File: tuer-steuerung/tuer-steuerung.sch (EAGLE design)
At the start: 47 parts, among them IC1 L6203, IC2 MEGA8-P, Q1 16Mhz, T1 BC337, T2 BC337

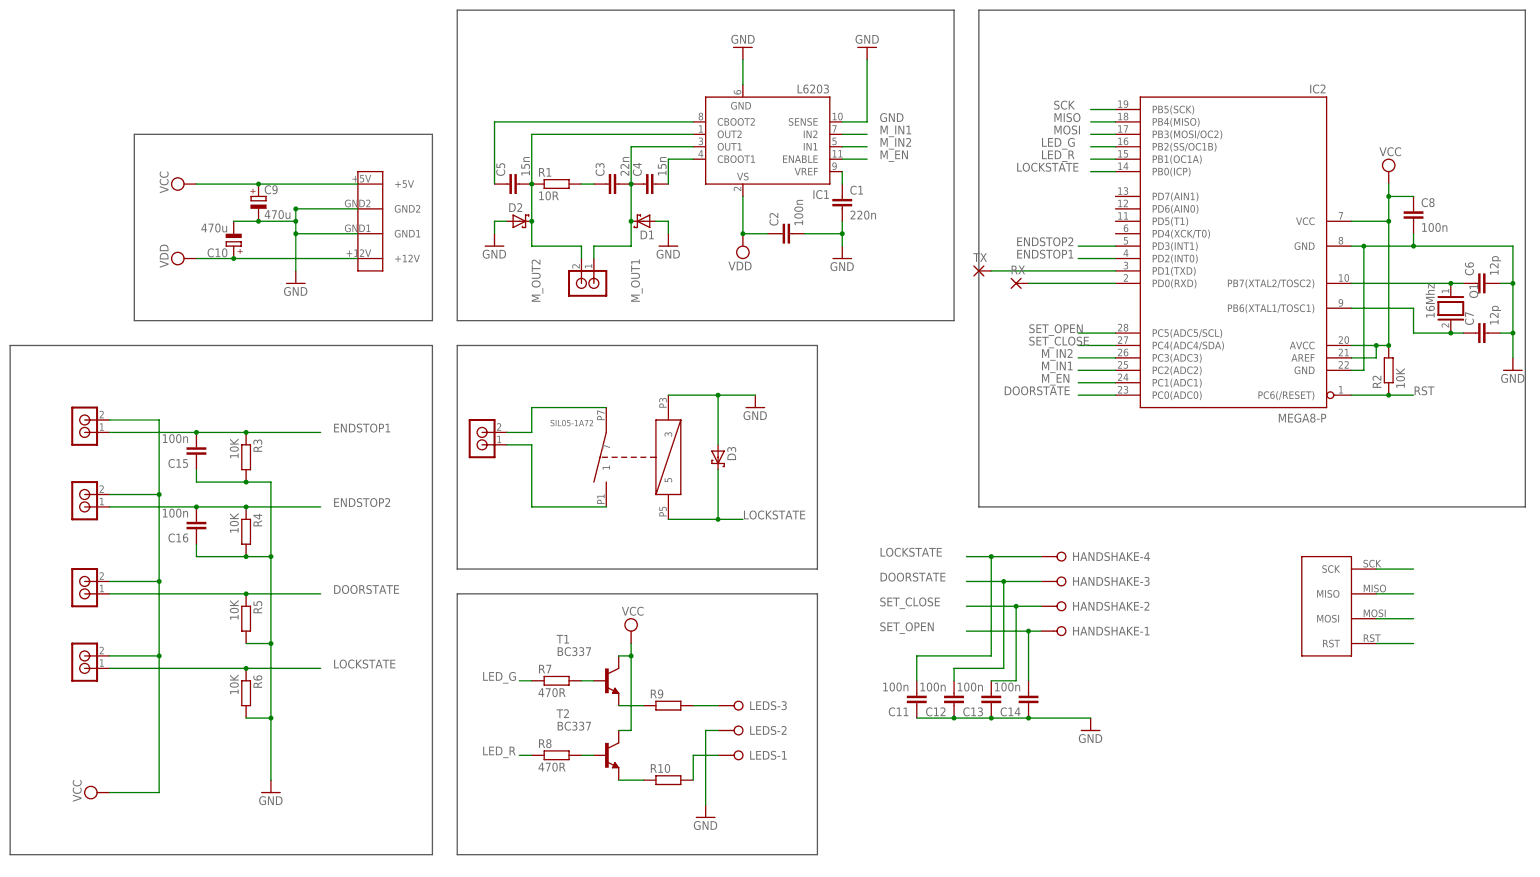
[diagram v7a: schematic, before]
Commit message: Anschlussklemmen durch die richtigen Typen ersetzt und Mini-Tweaks
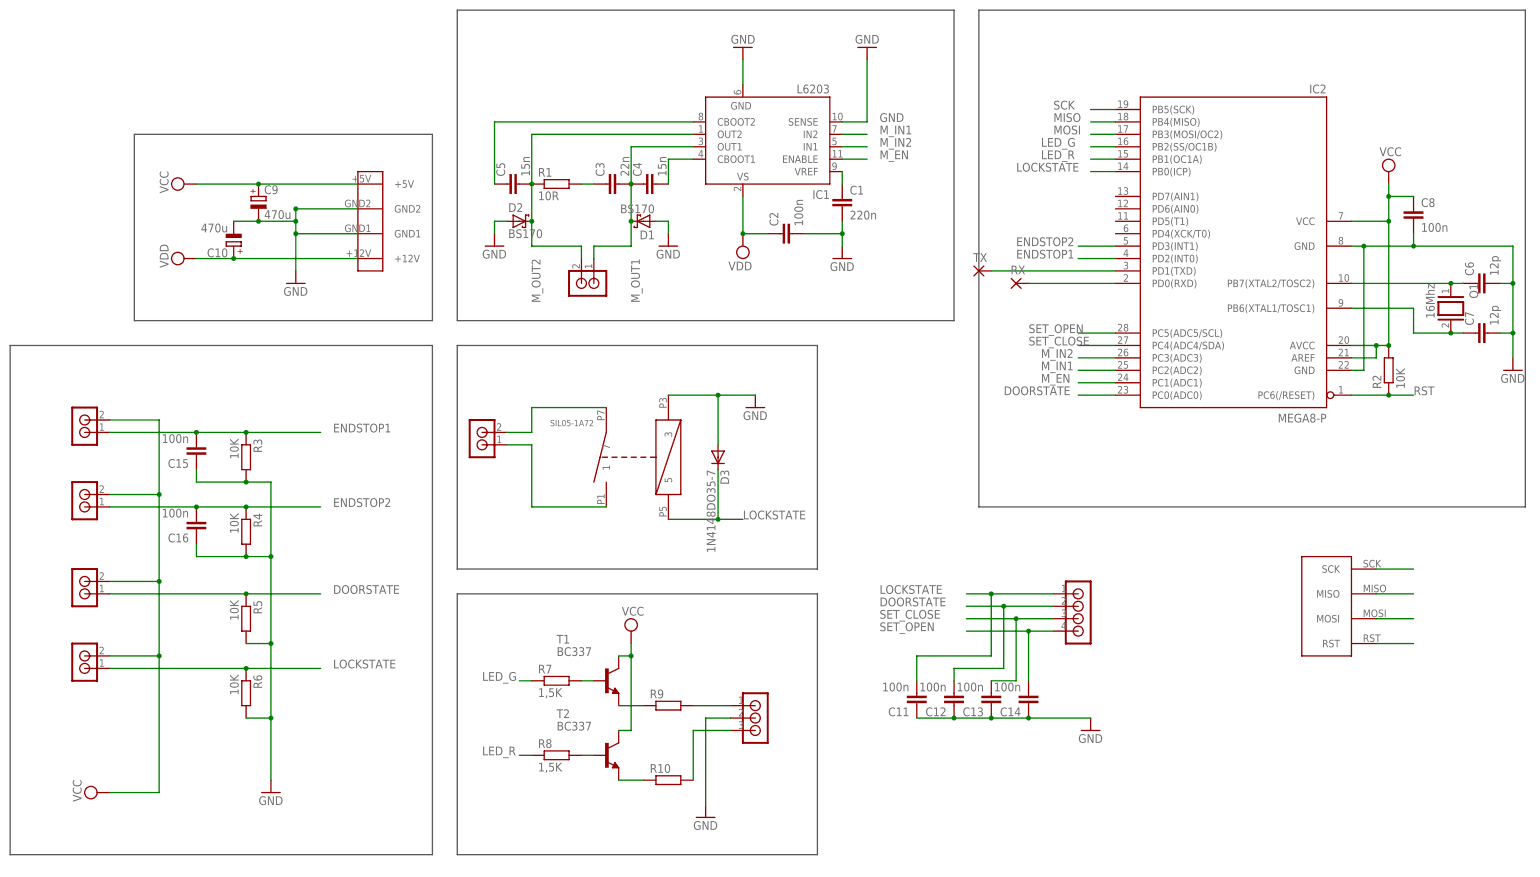
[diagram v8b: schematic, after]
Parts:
- removed HANDSHAKE: (no value), con-wago-508:W237-04P
- removed LEDS: (no value), con-wago-508:W237-03P
- added U$4: RIACON_101_3, n39:RIACON_101_3
- added U$5: RIACON_101_4, n39:RIACON_101_4
- D1, D2: value (none) -> BS170
- D3: value (none) -> 1N4148DO35-7; device diode:SCHOTTKY-DIODEDO35-7 -> diode:1N4148DO35-7
- R7, R8: value 470R -> 1,5K
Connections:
- net DOORSTATE: now also U$5.2; no longer HANDSHAKE-3.KL
- net GND: now also U$4.2; no longer LEDS-2.KL
- net LOCKSTATE: now also U$5.1; no longer HANDSHAKE-4.KL
- net N$12: now also U$4.1; no longer LEDS-3.KL
- net N$14: now also U$4.3; no longer LEDS-1.KL
- net SET_CLOSE: now also U$5.3; no longer HANDSHAKE-2.KL
- net SET_OPEN: now also U$5.4; no longer HANDSHAKE-1.KL
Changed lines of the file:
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@@
 <part name="IC2" library="atmel" deviceset="MEGA8-P" device=""/>
 <part name="Q1" library="special" deviceset="XTAL/S" device="" value="16Mhz"/>
-<part name="D1" library="diode" deviceset="SCHOTTKY-DIODE" device="DO35-7"/>
-<part name="D2" library="diode" deviceset="SCHOTTKY-DIODE" device="DO35-7"/>
+<part name="D1" library="diode" deviceset="SCHOTTKY-DIODE" device="DO35-7" value="BS170"/>
+<part name="D2" library="diode" deviceset="SCHOTTKY-DIODE" device="DO35-7" value="BS170"/>
 <part name="GND1" library="supply1" deviceset="GND" device=""/>
 <part name="SUPPLY1" library="supply2" deviceset="VDD" device=""/>
@@
 <part name="R6" library="resistor" deviceset="R-EU_" device="0204/5" value="10K"/>
 <part name="U$2" library="n39" deviceset="SIL05-1A72" device=""/>
-<part name="D3" library="diode" deviceset="SCHOTTKY-DIODE" device="DO35-7"/>
+<part name="D3" library="diode" deviceset="1N4148" device="DO35-7"/>
 <part name="GND9" library="supply1" deviceset="GND" device=""/>
 <part name="T1" library="transistor" deviceset="BC337" device=""/>
 <part name="T2" library="transistor" deviceset="BC337" device=""/>
-<part name="R7" library="resistor" deviceset="R-EU_" device="0204/5" value="470R"/>
-<part name="R8" library="resistor" deviceset="R-EU_" device="0204/5" value="470R"/>
-<part name="LEDS" library="con-wago-508" deviceset="W237-03P" device=""/>
+<part name="R7" library="resistor" deviceset="R-EU_" device="0204/5" value="1,5K"/>
+<part name="R8" library="resistor" deviceset="R-EU_" device="0204/5" value="1,5K"/>
 <part name="GND10" library="supply1" deviceset="GND" device=""/>
-<part name="HANDSHAKE" library="con-wago-508" deviceset="W237-04P" device=""/>
 <part name="R9" library="resistor" deviceset="R-EU_" device="0207/2V"/>
 <part name="R10" library="resistor" deviceset="R-EU_" device="0207/2V"/>
@@
 <part name="NERDSTERN" library="n39" deviceset="RIACON_101_2" device=""/>
 <part name="GND8" library="supply1" deviceset="GND" device=""/>
+<part name="U$4" library="n39" deviceset="RIACON_101_3" device=""/>
+<part name="U$5" library="n39" deviceset="RIACON_101_4" device=""/>
 </parts>
 <sheets>
@@
 <instance part="R7" gate="G$1" x="7.62" y="-66.04"/>
 <instance part="R8" gate="G$1" x="7.62" y="-81.28"/>
-<instance part="LEDS" gate="-1" x="45.72" y="-81.28" rot="R180"/>
-<instance part="LEDS" gate="-2" x="45.72" y="-76.2" rot="R180"/>
-<instance part="LEDS" gate="-3" x="45.72" y="-71.12" rot="R180"/>
 <instance part="GND10" gate="1" x="38.1" y="-93.98"/>
-<instance part="HANDSHAKE" gate="-1" x="111.76" y="-55.88" rot="R180"/>
-<instance part="HANDSHAKE" gate="-2" x="111.76" y="-50.8" rot="R180"/>
-<instance part="HANDSHAKE" gate="-3" x="111.76" y="-45.72" rot="R180"/>
-<instance part="HANDSHAKE" gate="-4" x="111.76" y="-40.64" rot="R180"/>
 <instance part="R9" gate="G$1" x="30.48" y="-71.12"/>
 <instance part="R10" gate="G$1" x="30.48" y="-86.36"/>
@@
 <instance part="NERDSTERN" gate="G$1" x="-7.62" y="-17.78" rot="R180"/>
 <instance part="GND8" gate="1" x="71.12" y="63.5" rot="R180"/>
+<instance part="U$4" gate="G$1" x="48.26" y="-73.66"/>
+<instance part="U$5" gate="G$1" x="114.3" y="-53.34"/>
 </instances>
 <busses>
@@
 <segment>
 <pinref part="GND10" gate="1" pin="GND"/>
-<wire x1="38.1" y1="-91.44" x2="38.1" y2="-76.2" width="0.1524" layer="91"/>
-<pinref part="LEDS" gate="-2" pin="KL"/>
-<wire x1="38.1" y1="-76.2" x2="40.64" y2="-76.2" width="0.1524" layer="91"/>
+<wire x1="38.1" y1="-91.44" x2="38.1" y2="-73.66" width="0.1524" layer="91"/>
+<pinref part="U$4" gate="G$1" pin="2"/>
+<wire x1="38.1" y1="-73.66" x2="43.18" y2="-73.66" width="0.1524" layer="91"/>
 </segment>
 <segment>
@@
 </segment>
 <segment>
-<pinref part="HANDSHAKE" gate="-3" pin="KL"/>
-<wire x1="106.68" y1="-45.72" x2="99.06" y2="-45.72" width="0.1524" layer="91"/>
-<label x="73.66" y="-45.72" size="1.778" layer="95"/>
+<wire x1="109.22" y1="-50.8" x2="99.06" y2="-50.8" width="0.1524" layer="91"/>
+<label x="73.66" y="-50.8" size="1.778" layer="95"/>
 <pinref part="C12" gate="G$1" pin="2"/>
-<wire x1="99.06" y1="-45.72" x2="91.44" y2="-45.72" width="0.1524" layer="91"/>
+<wire x1="99.06" y1="-50.8" x2="91.44" y2="-50.8" width="0.1524" layer="91"/>
 <wire x1="88.9" y1="-66.04" x2="88.9" y2="-63.5" width="0.1524" layer="91"/>
 <wire x1="88.9" y1="-63.5" x2="99.06" y2="-63.5" width="0.1524" layer="91"/>
-<wire x1="99.06" y1="-63.5" x2="99.06" y2="-45.72" width="0.1524" layer="91"/>
-<junction x="99.06" y="-45.72"/>
+<wire x1="99.06" y1="-63.5" x2="99.06" y2="-50.8" width="0.1524" layer="91"/>
+<junction x="99.06" y="-50.8"/>
+<pinref part="U$5" gate="G$1" pin="2"/>
 </segment>
 </net>
@@
 </segment>
 <segment>
-<pinref part="HANDSHAKE" gate="-4" pin="KL"/>
-<wire x1="106.68" y1="-40.64" x2="96.52" y2="-40.64" width="0.1524" layer="91"/>
-<label x="73.66" y="-40.64" size="1.778" layer="95"/>
+<wire x1="109.22" y1="-48.26" x2="96.52" y2="-48.26" width="0.1524" layer="91"/>
+<label x="73.66" y="-48.26" size="1.778" layer="95"/>
 <pinref part="C11" gate="G$1" pin="2"/>
-<wire x1="96.52" y1="-40.64" x2="91.44" y2="-40.64" width="0.1524" layer="91"/>
+<wire x1="96.52" y1="-48.26" x2="91.44" y2="-48.26" width="0.1524" layer="91"/>
 <wire x1="81.28" y1="-66.04" x2="81.28" y2="-60.96" width="0.1524" layer="91"/>
 <wire x1="81.28" y1="-60.96" x2="96.52" y2="-60.96" width="0.1524" layer="91"/>
-<wire x1="96.52" y1="-60.96" x2="96.52" y2="-40.64" width="0.1524" layer="91"/>
-<junction x="96.52" y="-40.64"/>
+<wire x1="96.52" y1="-60.96" x2="96.52" y2="-48.26" width="0.1524" layer="91"/>
+<junction x="96.52" y="-48.26"/>
+<pinref part="U$5" gate="G$1" pin="1"/>
 </segment>
 <segment>
@@
 <net name="SET_OPEN" class="0">
 <segment>
-<pinref part="HANDSHAKE" gate="-1" pin="KL"/>
-<wire x1="106.68" y1="-55.88" x2="104.14" y2="-55.88" width="0.1524" layer="91"/>
 <label x="73.66" y="-55.88" size="1.778" layer="95"/>
 <pinref part="C14" gate="G$1" pin="2"/>
@@
 <wire x1="104.14" y1="-66.04" x2="104.14" y2="-55.88" width="0.1524" layer="91"/>
 <junction x="104.14" y="-55.88"/>
+<pinref part="U$5" gate="G$1" pin="4"/>
+<wire x1="104.14" y1="-55.88" x2="109.22" y2="-55.88" width="0.1524" layer="91"/>
 </segment>
 <segment>
@@
 </segment>
 <segment>
-<pinref part="HANDSHAKE" gate="-2" pin="KL"/>
-<wire x1="106.68" y1="-50.8" x2="101.6" y2="-50.8" width="0.1524" layer="91"/>
-<label x="73.66" y="-50.8" size="1.778" layer="95"/>
+<wire x1="109.22" y1="-53.34" x2="101.6" y2="-53.34" width="0.1524" layer="91"/>
+<label x="73.66" y="-53.34" size="1.778" layer="95"/>
 <pinref part="C13" gate="G$1" pin="2"/>
-<wire x1="101.6" y1="-50.8" x2="91.44" y2="-50.8" width="0.1524" layer="91"/>
+<wire x1="101.6" y1="-53.34" x2="91.44" y2="-53.34" width="0.1524" layer="91"/>
 <wire x1="96.52" y1="-66.04" x2="101.6" y2="-66.04" width="0.1524" layer="91"/>
-<wire x1="101.6" y1="-66.04" x2="101.6" y2="-50.8" width="0.1524" layer="91"/>
-<junction x="101.6" y="-50.8"/>
+<wire x1="101.6" y1="-66.04" x2="101.6" y2="-53.34" width="0.1524" layer="91"/>
+<junction x="101.6" y="-53.34"/>
+<pinref part="U$5" gate="G$1" pin="3"/>
 </segment>
 </net>
@@
 <segment>
 <pinref part="R9" gate="G$1" pin="2"/>
-<pinref part="LEDS" gate="-3" pin="KL"/>
-<wire x1="35.56" y1="-71.12" x2="40.64" y2="-71.12" width="0.1524" layer="91"/>
+<wire x1="35.56" y1="-71.12" x2="43.18" y2="-71.12" width="0.1524" layer="91"/>
+<pinref part="U$4" gate="G$1" pin="1"/>
 </segment>
 </net>
@@
 <segment>
 <pinref part="R10" gate="G$1" pin="2"/>
-<wire x1="35.56" y1="-86.36" x2="35.56" y2="-81.28" width="0.1524" layer="91"/>
-<pinref part="LEDS" gate="-1" pin="KL"/>
-<wire x1="35.56" y1="-81.28" x2="40.64" y2="-81.28" width="0.1524" layer="91"/>
-</segment>
-</net>
+<wire x1="35.56" y1="-86.36" x2="35.56" y2="-76.2" width="0.1524" layer="91"/>
+<wire x1="35.56" y1="-76.2" x2="43.18" y2="-76.2" width="0.1524" layer="91"/>
+<pinref part="U$4" gate="G$1" pin="3"/>
+</segment>
+</net>
